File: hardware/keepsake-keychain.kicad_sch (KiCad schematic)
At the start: 93 parts, among them Q1 MMFTP4042K, Q2 MMFTP4042K, Q3 MMFTP4042K, Q4 MMFTP4042K, SW1 SPDT Power Switch, SW2 PTS636 SK25J SMTR LFS, U1 74HC595 BLUE Shift Register, U2 74HC595 GREEN Shift Register, U3 74HC595 RED Shift Register, U4 ATTINY1614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

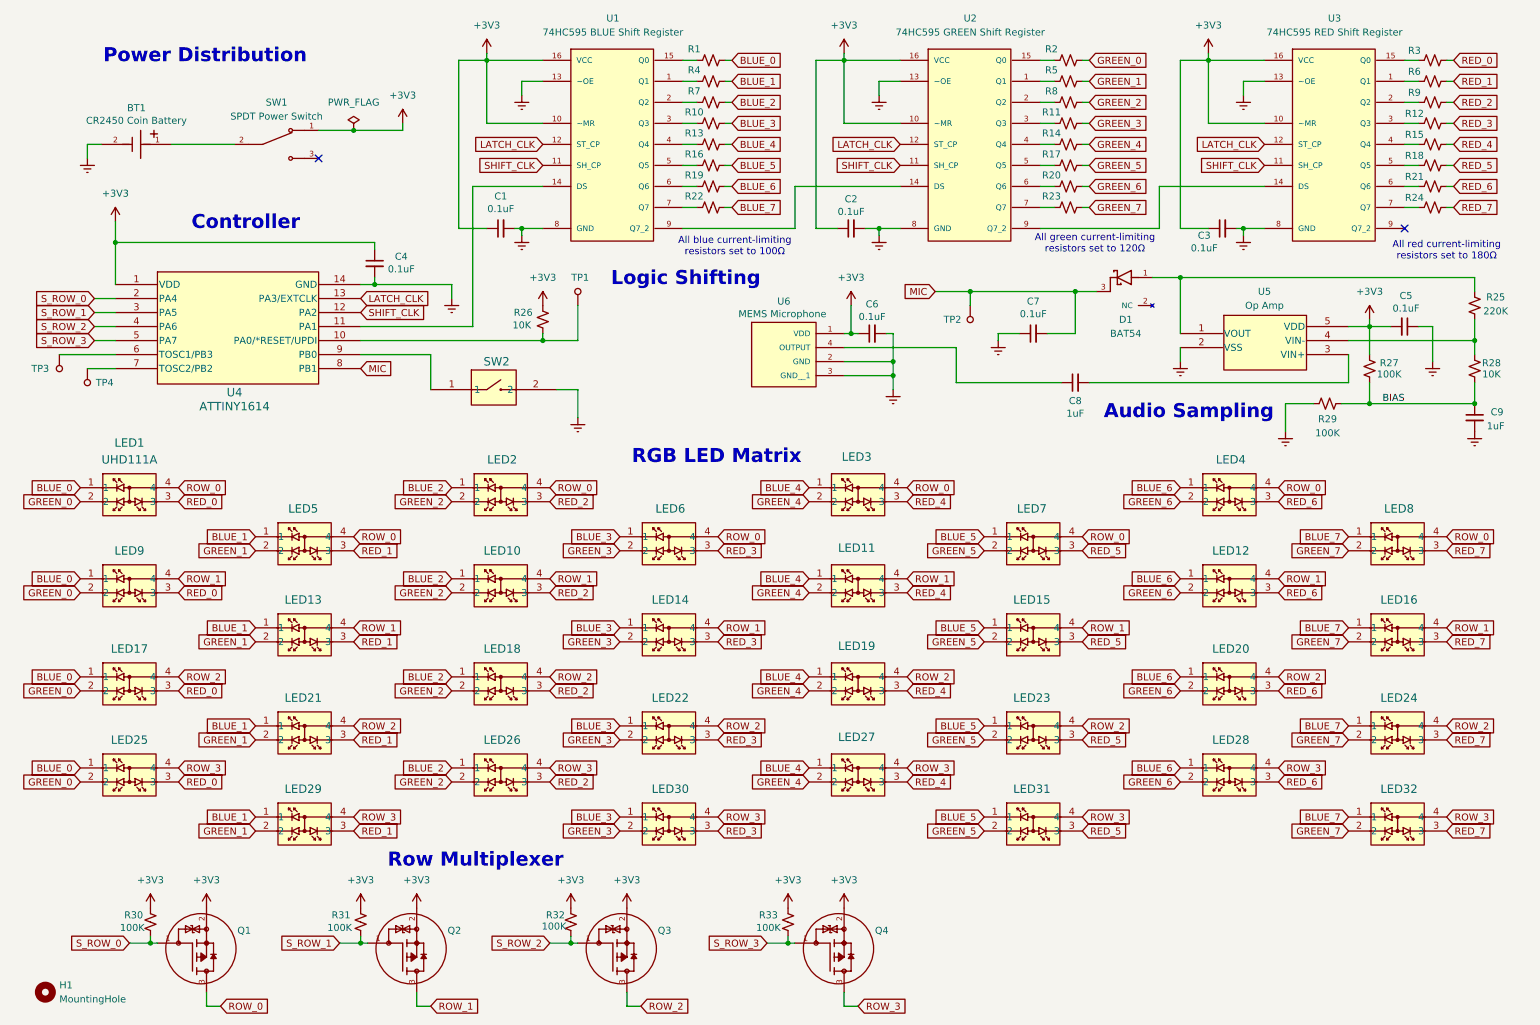
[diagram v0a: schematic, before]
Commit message: Place LED passives in line
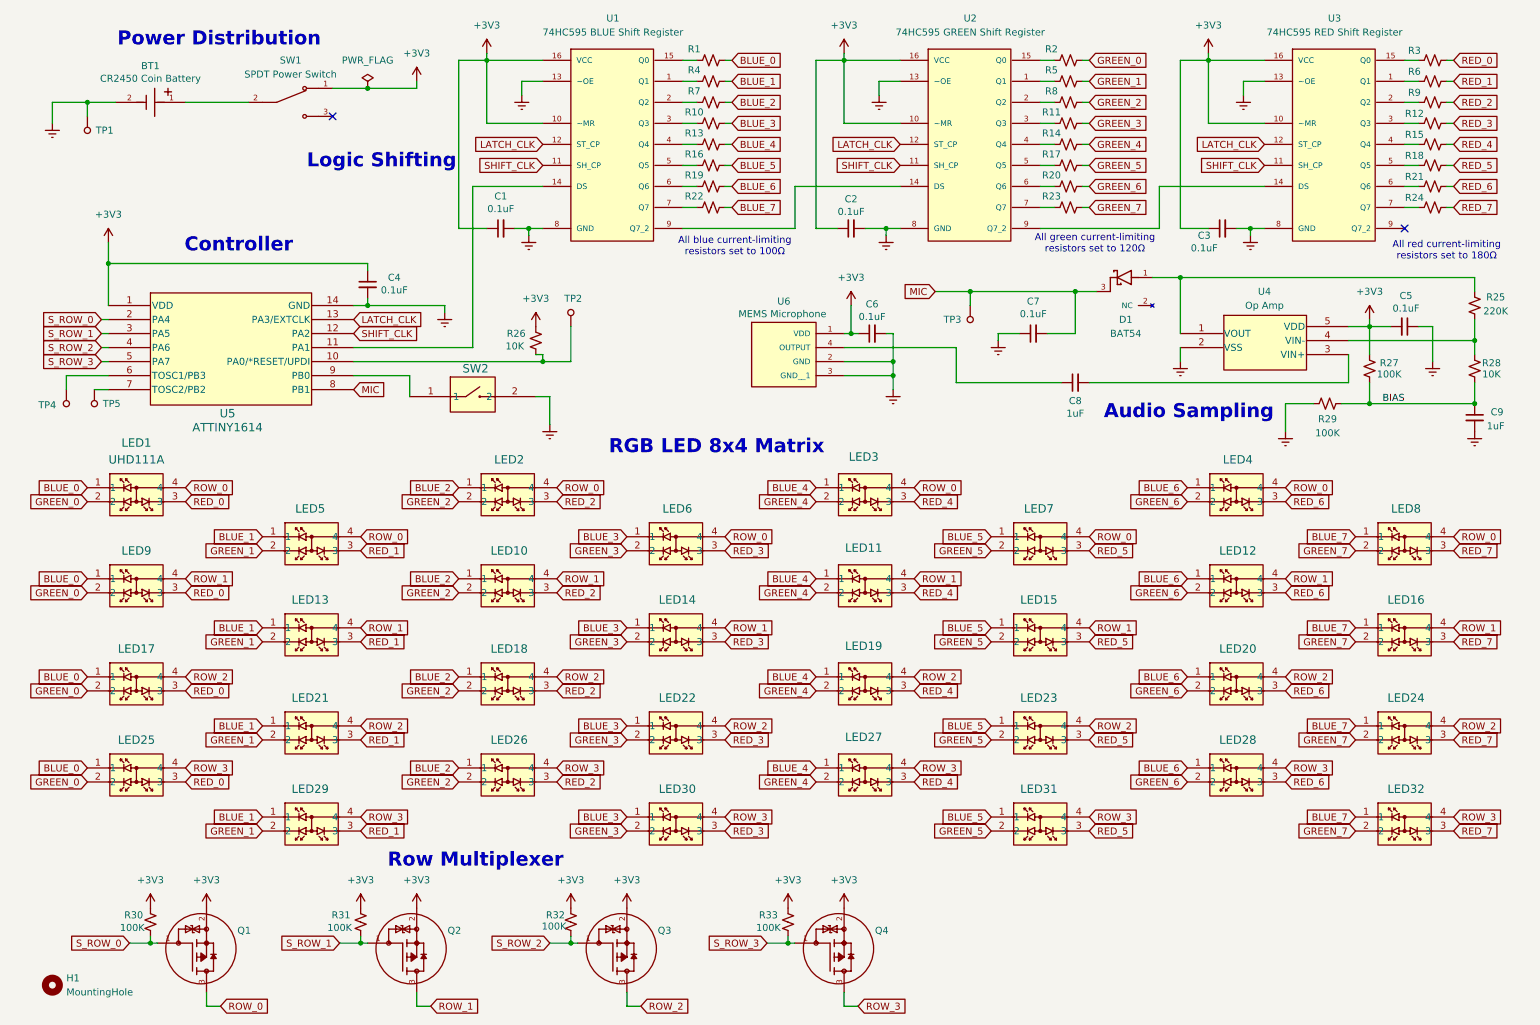
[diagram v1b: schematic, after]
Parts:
- added TP1: 5002, digikey-footprints:Test_Point_D1.02mm, symbol dk_Test-Points:5002
- renumbered TP1 to TP2, TP2 to TP3, TP3 to TP4, TP4 to TP5, U5 to U4, U4 to U5
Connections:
- net GND: now also TP1.1
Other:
- note added: "RGB LED 8x4 Matrix"
- note removed: "RGB LED Matrix"
- moved on the sheet: BT1, C4, H1, LED1, LED10, LED11, LED12, LED13, LED14, LED15, LED16, LED17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

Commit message: Rename nets, move resistors to rear
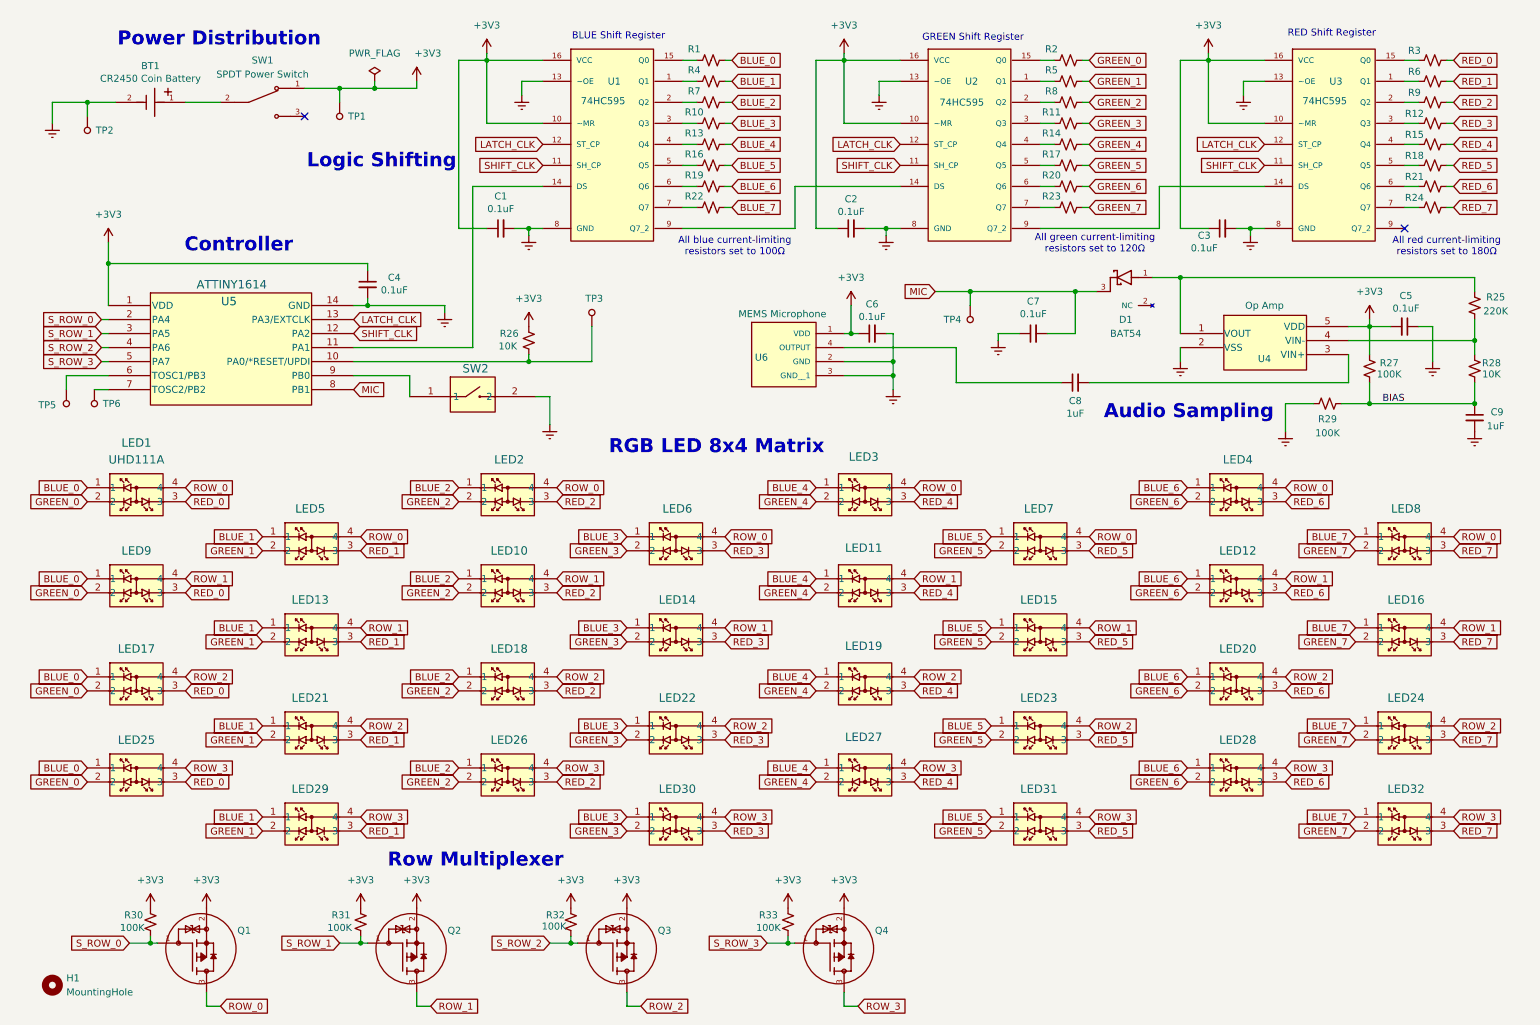
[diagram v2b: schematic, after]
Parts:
- added TP1: 5002, TestPoint:TestPoint_THTPad_D1.5mm_Drill0.7mm, symbol dk_Test-Points:5002
- TP2: renamed from TP1; footprint digikey-footprints:Test_Point_D1.02mm -> TestPoint:TestPoint_THTPad_D1.5mm_Drill0.7mm
- TP3: renamed from TP2; footprint digikey-footprints:Test_Point_D1.02mm -> TestPoint:TestPoint_THTPad_D1.5mm_Drill0.7mm
- TP4: renamed from TP3; footprint digikey-footprints:Test_Point_D1.02mm -> TestPoint:TestPoint_THTPad_D1.5mm_Drill0.7mm
- TP5: renamed from TP4; footprint digikey-footprints:Test_Point_D1.02mm -> TestPoint:TestPoint_THTPad_D1.5mm_Drill0.7mm
- TP6: renamed from TP5; footprint digikey-footprints:Test_Point_D1.02mm -> TestPoint:TestPoint_THTPad_D1.5mm_Drill0.7mm
- U1: value 74HC595 BLUE Shift Register -> 74HC595
- U2: value 74HC595 GREEN Shift Register -> 74HC595
- U3: value 74HC595 RED Shift Register -> 74HC595
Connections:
- net +3V3: now also TP1.1
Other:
- note added: "BLUE Shift Register"
- note added: "GREEN Shift Register"
- note added: "RED Shift Register"
- moved on the sheet: R26, SW1, TP3

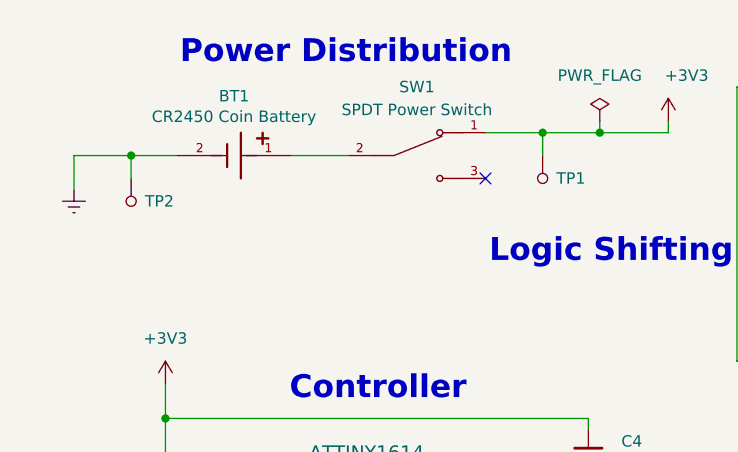
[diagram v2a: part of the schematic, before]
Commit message: Fix broken net, fix via annular ring constraint
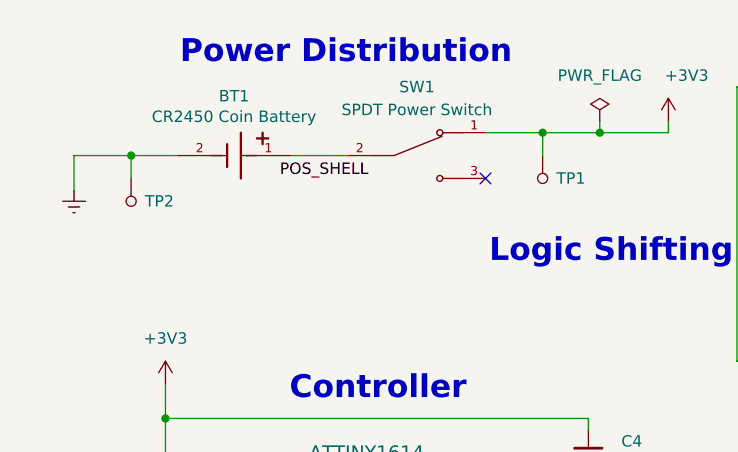
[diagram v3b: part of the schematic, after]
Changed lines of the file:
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@@
+		)
+	)
+	(label "POS_SHELL"
+		(at 41.91 33.02 0)
+		(effects
+			(font
+				(size 1.27 1.27)
+			)
+			(justify left bottom)
 		)
 	)

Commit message: Place remaining passives
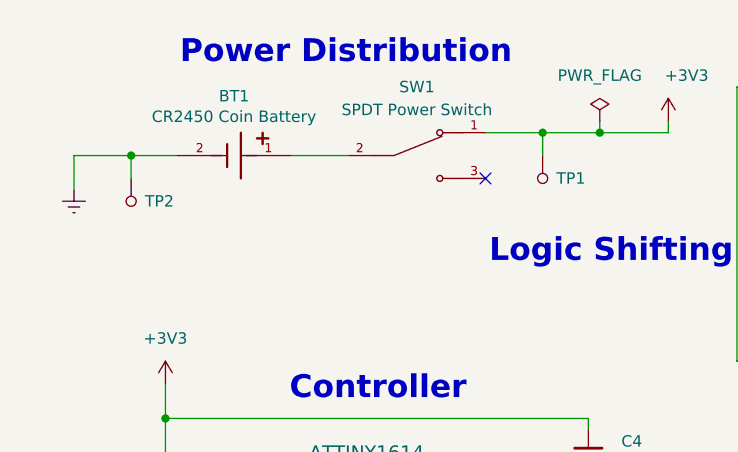
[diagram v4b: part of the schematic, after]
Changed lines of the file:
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@@
 		(rev "1")
 		(comment 2 "             given away during Eric & Stephie's wedding.")
-		(comment 3 "Description: A 100mm by 30mm RGB LED matrix keychain")
+		(comment 3 "Description: An 80mm by 30mm RGB LED matrix keychain")
 		(comment 4 "Author:      Eric McDanel")
 	)
@@
 		)
 	)
-	(label "POS_SHELL"
-		(at 41.91 33.02 0)
-		(effects
-			(font
-				(size 1.27 1.27)
-			)
-			(justify left bottom)
-		)
-	)
